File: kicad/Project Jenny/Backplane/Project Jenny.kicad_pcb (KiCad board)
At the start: 4 copper layers, 198.1 x 198.1 mm, 54 parts, among them J1 Conn_01x04

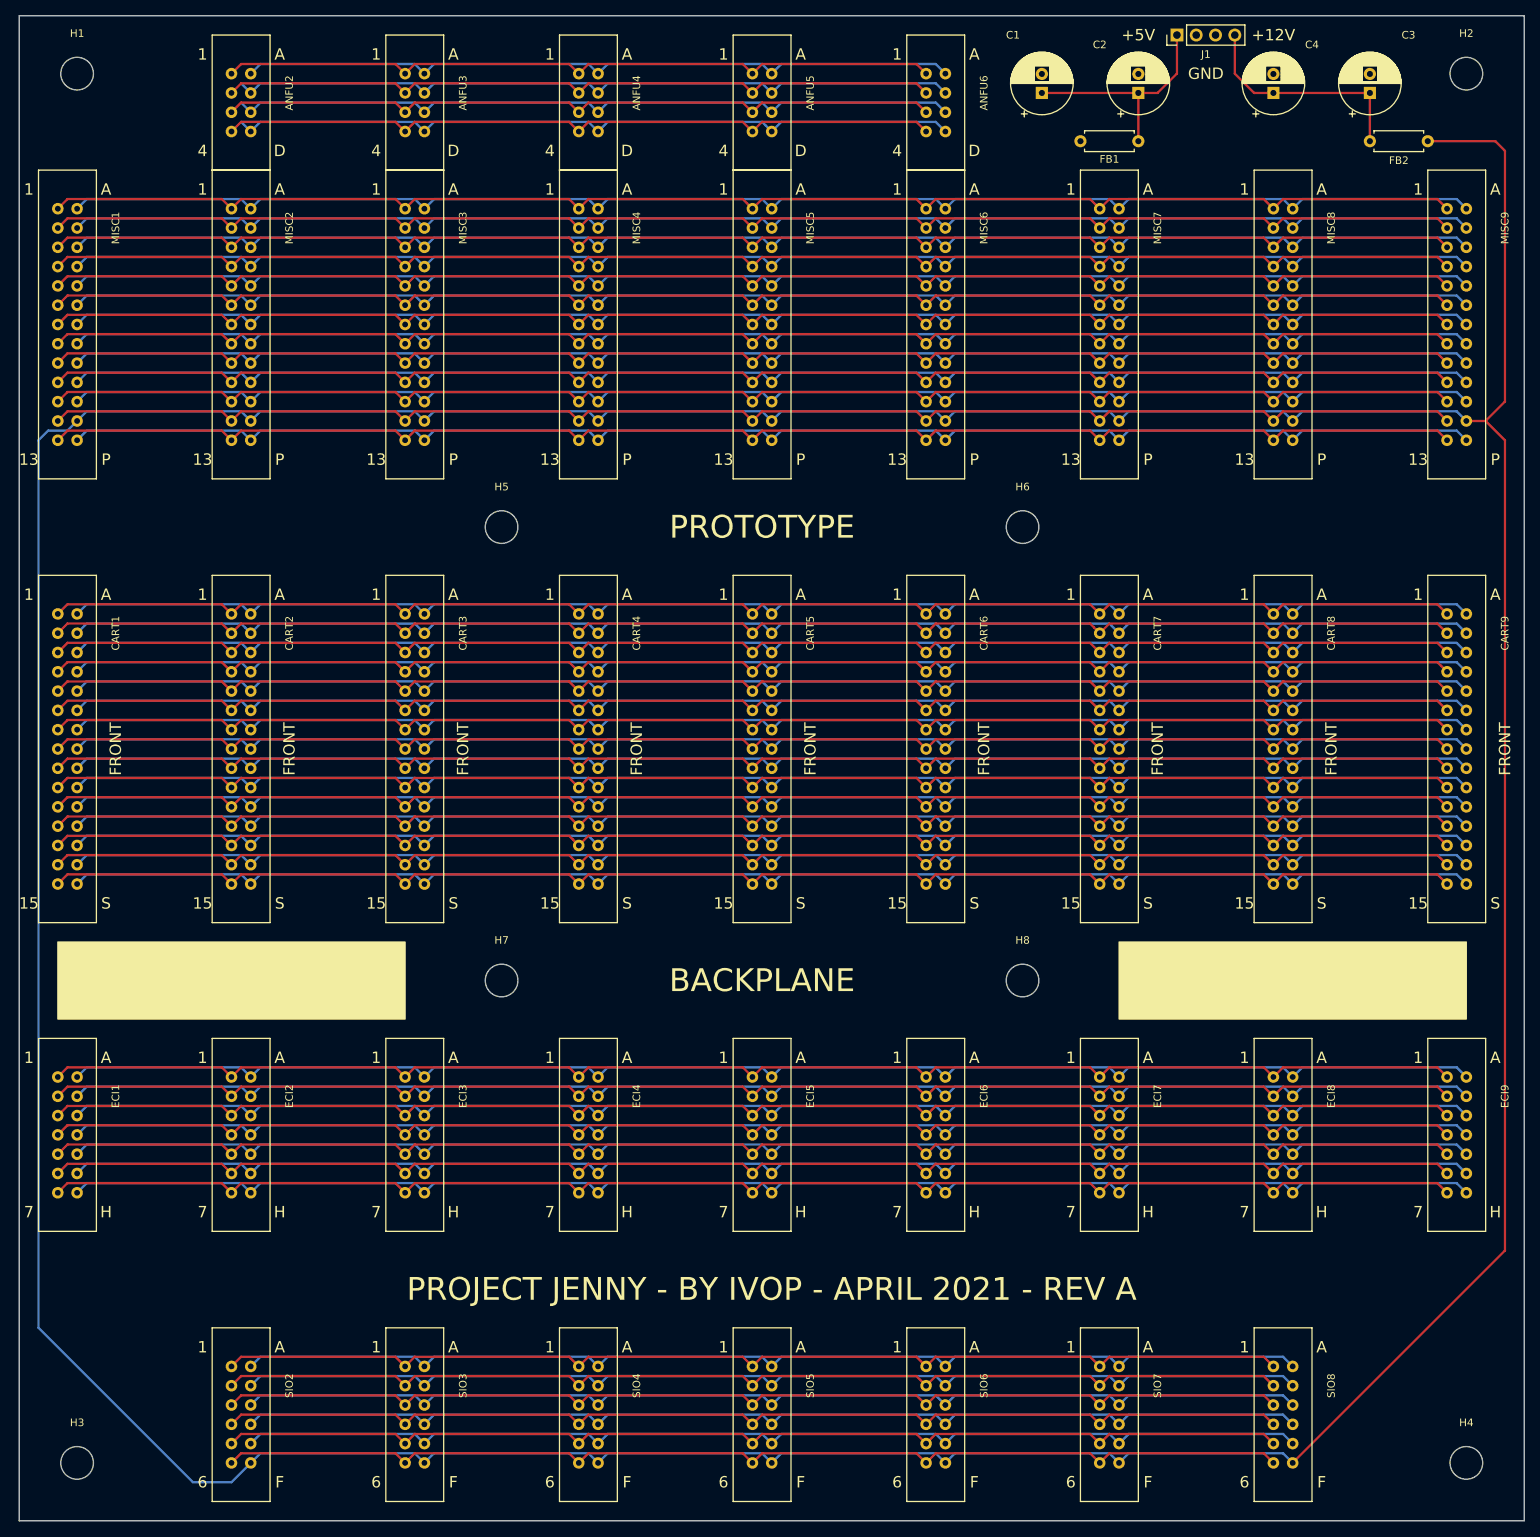
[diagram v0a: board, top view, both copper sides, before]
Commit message: add LED lights for +5V and +12V
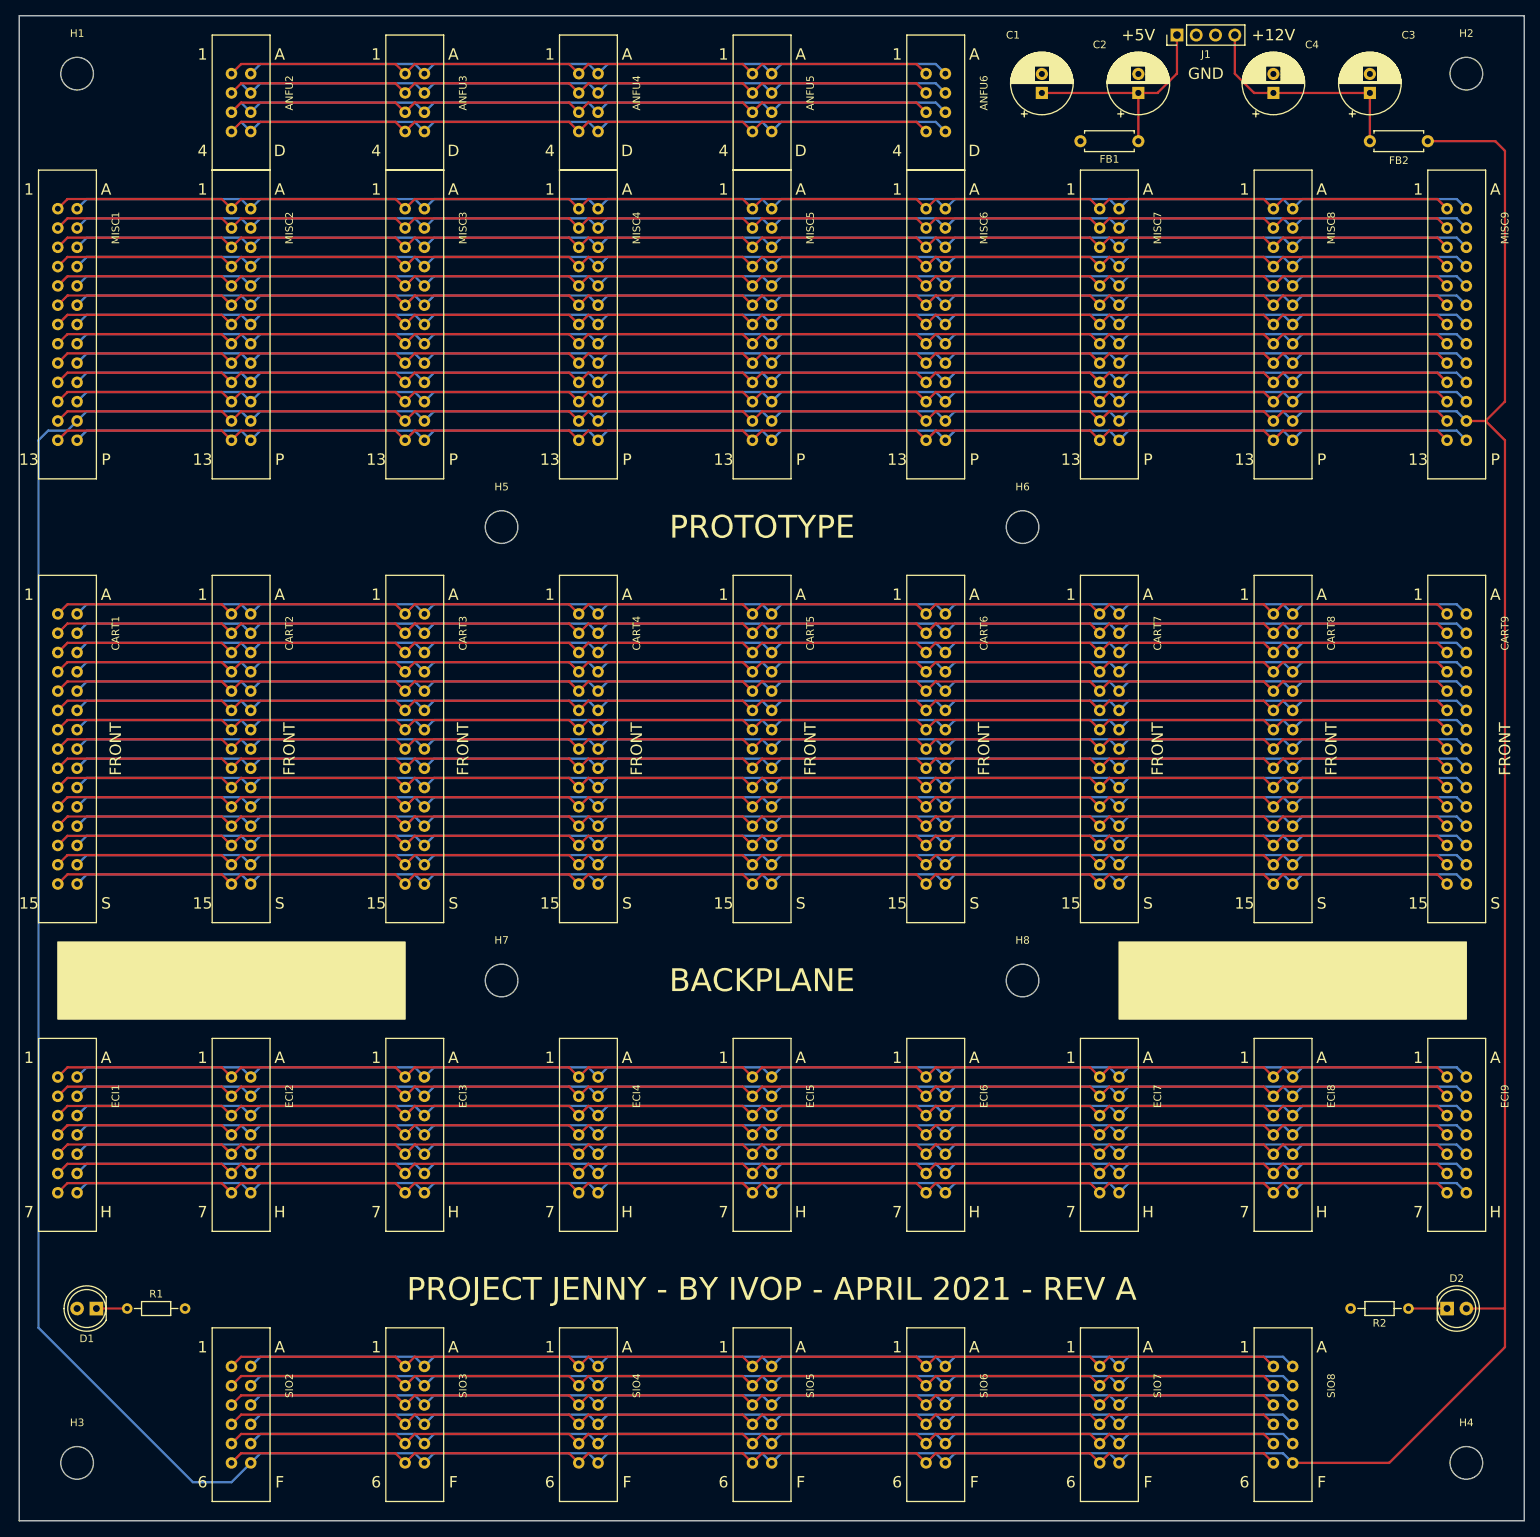
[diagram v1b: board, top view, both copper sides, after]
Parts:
- added D1: LED, LED_THT:LED_D5.0mm, F.Cu at (43.2, 208.3)
- added D2: LED, LED_THT:LED_D5.0mm, F.Cu at (221.0, 208.3)
- added R1: 470, Resistor_THT:R_Axial_DIN0204_L3.6mm_D1.6mm_P7.62mm_Horizontal, F.Cu at (47.2, 208.3)
- added R2: 1K5, Resistor_THT:R_Axial_DIN0204_L3.6mm_D1.6mm_P7.62mm_Horizontal, F.Cu at (215.9, 208.3)
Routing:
- net +12V: track 694.8 -> 707.3 mm
- net Net-(D2-Pad1): track 0.00 -> 5.08 mm
- net Net-(D1-Pad1): track 0.00 -> 4.05 mm
